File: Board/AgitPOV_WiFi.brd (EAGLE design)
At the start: 41.5 x 67.6 mm, 45 parts, among them U1 MMA8452Q

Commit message: Mean and lean board
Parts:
- removed HALL: Hall, SparkFun-Connectors:1X03
- removed JP-GND: SWITCH, SparkFun-Connectors:1X01
- removed JP-GNDE: -, SparkFun-Connectors:1X01
- removed PUSHBUTTON: (no value), switch-omron:B3F-10XX
- removed R3: 10k, SparkFun-Resistors:1206
- added U$1: SWITCH_SPDT, SparkFun-Electromechanical:KPS-1290
- moved BATT 19.5 mm to (5.01, 24.1), turned to 0 degrees
- moved JST 17.3 mm to (3.90, 20.8), turned to 270 degrees
- moved DEL1 4.60 mm to (32.4, 4.74)
- moved DEL10 4.60 mm to (32.5, 53.0)
- moved DEL11 4.60 mm to (32.5, 58.3)
- moved DEL12 4.60 mm to (32.5, 63.6)
- moved DEL13 4.60 mm to (32.5, 63.6)
- moved DEL15 4.60 mm to (32.5, 53.0)
- moved DEL17 4.60 mm to (32.5, 42.4)
- moved DEL18 4.60 mm to (32.5, 37.0)
- moved DEL19 4.60 mm to (32.5, 31.7)
- moved DEL2 4.60 mm to (32.5, 10.1)
- moved DEL20 4.60 mm to (32.5, 26.4)
- moved DEL21 4.60 mm to (32.5, 21.1)
- moved DEL22 4.60 mm to (32.5, 15.8)
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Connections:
- removed net PULLDOWN: PUSHBUTTON.3, R3.2, WEMOS1.3
- removed net SA0: U1.7, WEMOS1.6
- net +3.3V: no longer HALL.1, PUSHBUTTON.1
- net ENTREEGND: now also U$1.S; no longer JP-GNDE.1
- net GND: now also U$1.P; no longer HALL.2, JP-GND.1, R3.1
- net N$41: no longer HALL.3
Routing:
- net PULLDOWN: track 28.9 -> 0.00 mm
- net SA0: track 23.5 -> 0.00 mm, vias 2 -> 0
- net 5V: track 284.5 -> 262.4 mm
- net GND: track 348.7 -> 332.9 mm, vias 0 -> 1
- net N$41: track 12.1 -> 0.00 mm
- net N$2: track 46.6 -> 40.8 mm
- net +3.3V: track 55.0 -> 49.2 mm
- net N$4: track 47.1 -> 41.6 mm
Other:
- board size 41.5 x 67.6 mm -> 37.2 x 67.7 mm
- board text removed: "D0"
- board text removed: "D8"
- board text removed: "R1"

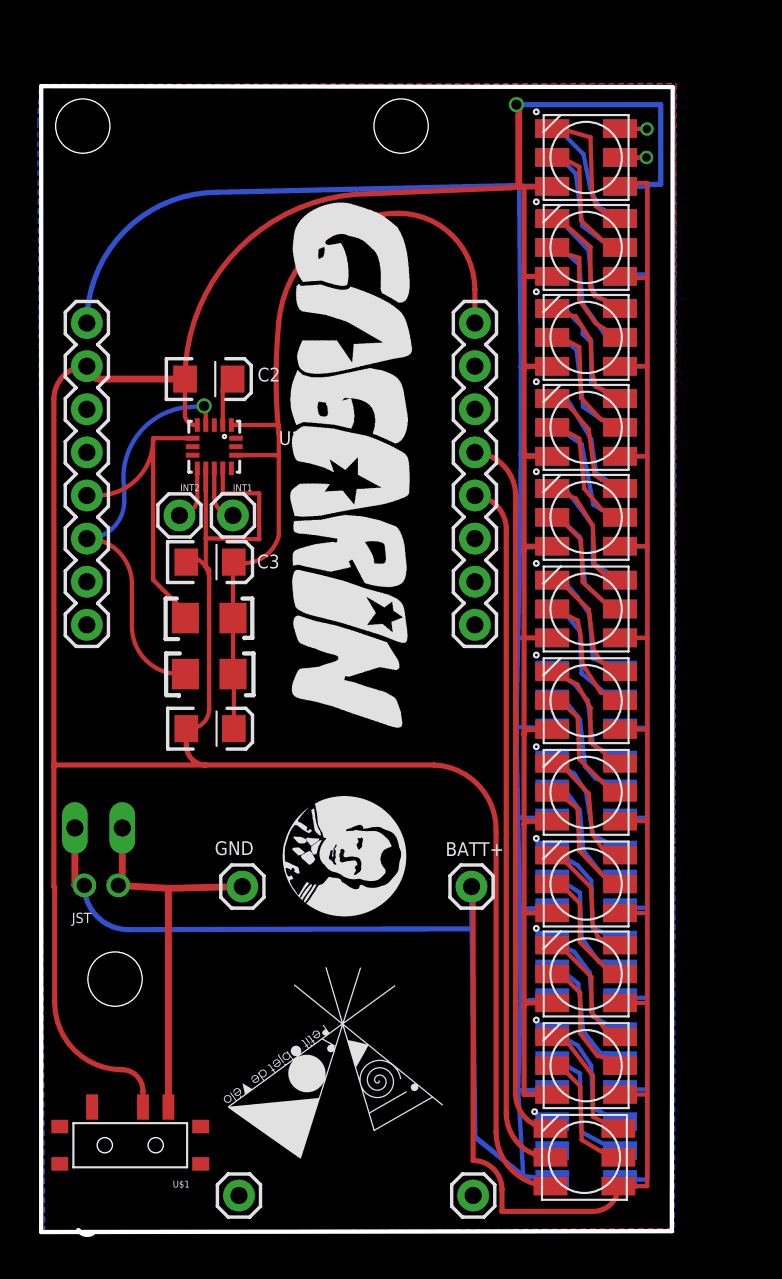
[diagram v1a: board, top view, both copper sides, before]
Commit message: Ajustement pour le tableau des caractères spéciaux
Nouveau board
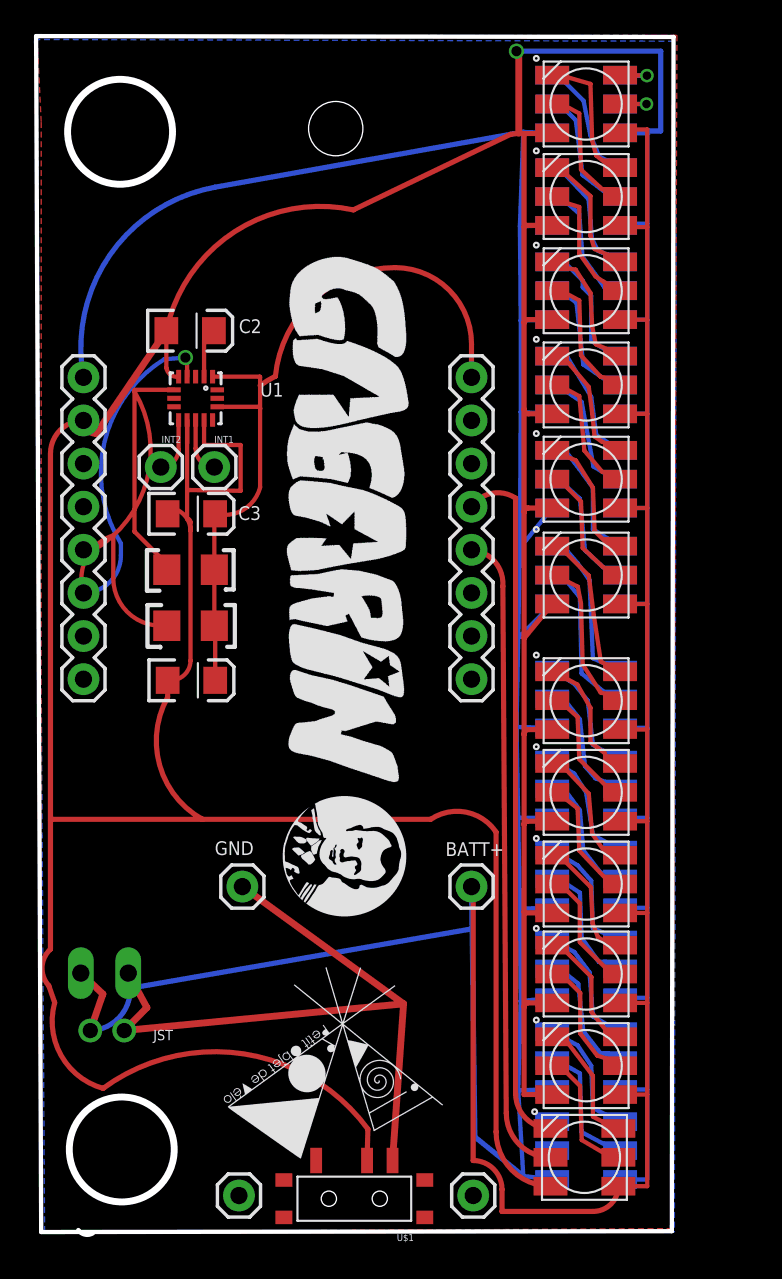
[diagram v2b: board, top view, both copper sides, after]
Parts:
- moved U$1 13.6 mm to (18.8, 2.30)
- moved BATT 8.56 mm to (5.36, 15.6)
- moved JST 8.56 mm to (4.25, 12.2)
- moved WEMOS2 3.21 mm to (2.84, 50.7)
- moved WEMOS1 3.21 mm to (25.7, 32.9)
- moved DEL12 3.15 mm to (32.5, 66.8)
- moved DEL13 3.15 mm to (32.5, 66.8)
- moved C3 3.05 mm to (9.20, 42.6)
- moved U1 3.05 mm to (9.45, 49.5)
- moved C1 3.05 mm to (9.20, 32.8)
- moved C2 3.05 mm to (9.13, 53.4)
- moved INT1 3.05 mm to (10.6, 45.4)
- moved INT2 3.05 mm to (7.40, 45.4)
- moved R2 3.05 mm to (9.15, 36.1)
- moved R1 3.05 mm to (9.15, 39.4)
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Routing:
- net GND: track 332.9 -> 358.5 mm
- net ENTREEGND: track 23.8 -> 41.7 mm
- net 5V: track 262.4 -> 273.9 mm
- net +3.3V: track 49.2 -> 43.7 mm
- net SCL: track 22.8 -> 28.1 mm
- net SDA: track 19.0 -> 24.0 mm
- net N$2: track 40.8 -> 37.6 mm
- net N$54: track 7.63 -> 9.63 mm
- net N$24: track 7.52 -> 9.52 mm
- net N$53: track 7.45 -> 9.44 mm
- net N$23: track 7.37 -> 9.29 mm
- net N$4: track 41.6 -> 40.6 mm
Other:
- board size 37.2 x 67.7 mm -> 37.6 x 70.6 mm

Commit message: New board version, FastLED display works.
Board : removed button, Hall sensor, back to smd switch, cleaning
around the accelerometer, removed int1 + int2, one less via! More space
for the LEDs -> resized board.
FastLED : correct GRB color space, bizarro world to display text on
both sides.
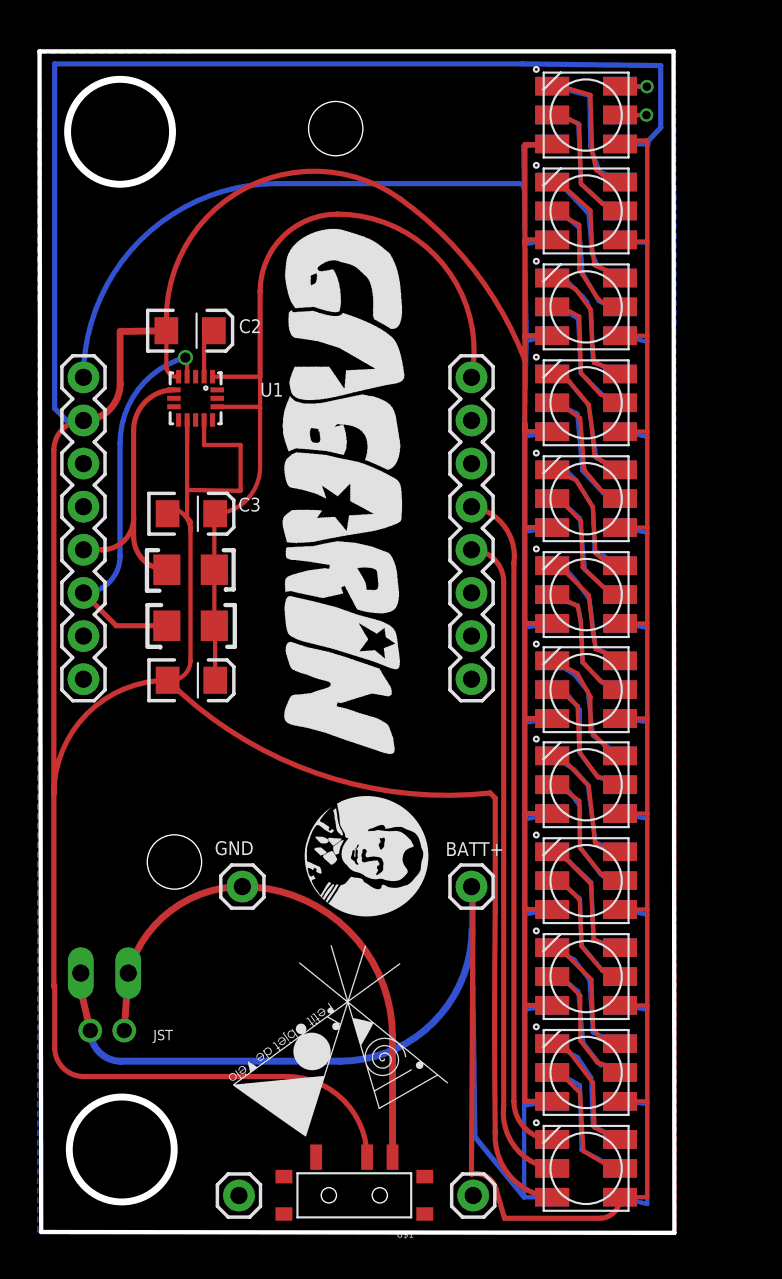
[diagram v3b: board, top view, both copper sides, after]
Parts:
- removed INT1, INT2: (no value), SparkFun-Connectors:1X01
- moved DEL17 1.15 mm to (32.5, 43.5)
- moved DEL18 1.15 mm to (32.5, 37.9)
- moved DEL7 1.15 mm to (32.5, 37.9)
- moved DEL8 1.15 mm to (32.5, 43.5)
- moved DEL24 1.05 mm to (32.5, 4.09)
- moved DEL16 1.05 mm to (32.5, 49.2)
- moved DEL9 1.05 mm to (32.5, 49.2)
- moved DEL10 0.95 mm to (32.5, 54.8)
- moved DEL15 0.95 mm to (32.5, 54.8)
- moved DEL11 0.85 mm to (32.5, 60.5)
- moved FFFFF 0.85 mm to (32.5, 60.5)
- moved DEL23 0.70 mm to (32.5, 9.74)
- moved DEL1 0.66 mm to (32.5, 4.09)
- moved DEL12 0.65 mm to (32.5, 66.1)
- moved DEL13 0.65 mm to (32.5, 66.1)
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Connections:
- net N$65: no longer INT1.1
- net N$67: no longer INT2.1
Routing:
- net GND: track 358.5 -> 405.3 mm, vias 1 -> 0
- net ENTREEGND: track 41.7 -> 31.4 mm
- net SDA: track 24.0 -> 16.1 mm
- net SCL: track 28.1 -> 22.9 mm
- net +3.3V: track 43.7 -> 48.3 mm
- net N$65: track 3.23 -> 0.00 mm
- net N$67: track 3.21 -> 0.00 mm
- net 5V: track 273.9 -> 271.4 mm
- net N$53: track 9.44 -> 7.57 mm
- net N$54: track 9.63 -> 7.92 mm
- net N$24: track 9.52 -> 7.82 mm
- net N$23: track 9.29 -> 7.68 mm
- net N$4: track 40.6 -> 39.0 mm
- net N$45: track 7.38 -> 8.32 mm
- net N$2: track 37.6 -> 38.2 mm
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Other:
- board size 37.6 x 70.6 mm -> 37.4 x 69.6 mm
- board text added: "R1"
- board text removed: "R3"
